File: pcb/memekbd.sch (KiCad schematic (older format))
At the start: 194 parts, among them J1 MJ-4PP-9, J2 MJ-4PP-9, SW1 SW_Push, SW10 SW_Push, SW11 SW_Push, SW12 SW_Push, SW13 SW_Push, SW14 SW_Push, SW15 SW_Push, SW16 SW_Push, SW17 SW_Push, SW18 SW_Push, SW19 SW_Push, SW2 SW_Push, SW20 SW_Push, SW21 SW_Push, SW22 SW_Push, SW23 SW_Push, SW24 SW_Push, SW25 SW_Push, SW26 SW_Push, SW27 SW_Push, SW28 SW_Push, SW29 SW_Push, SW3 SW_Push, SW30 SW_Push, SW31 SW_Push, SW32 SW_Push, SW33 SW_Push, SW34 SW_Push, SW35 SW_Push, SW36 SW_Push, SW37 SW_Push, SW38 SW_Push, SW39 SW_Push, SW4 SW_Push, SW40 SW_Push, SW41 SW_Push, SW42 SW_Push, SW43 SW_Push, SW44 SW_Push, SW45 SW_Push, SW46 SW_Push, SW47 SW_Push, SW48 SW_Push, SW5 SW_Push, SW6 SW_Push, SW7 SW_Push, SW8 SW_Push, SW9 SW_Push, U1 ProMicro, U2 ProMicro

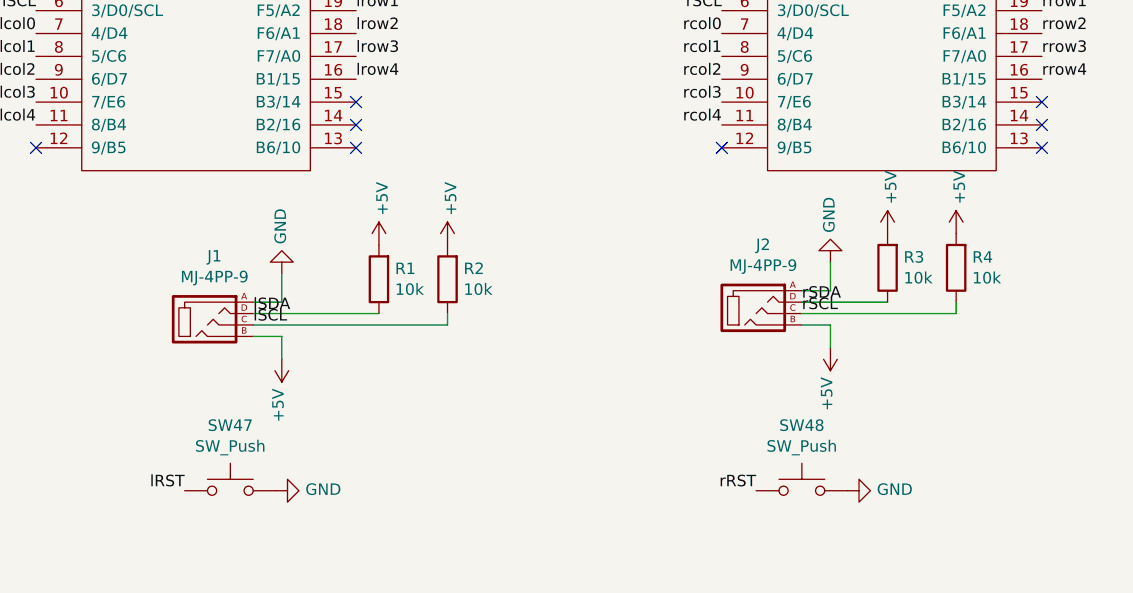
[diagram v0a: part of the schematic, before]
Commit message: Remove unnecessary libraries. Update footprints
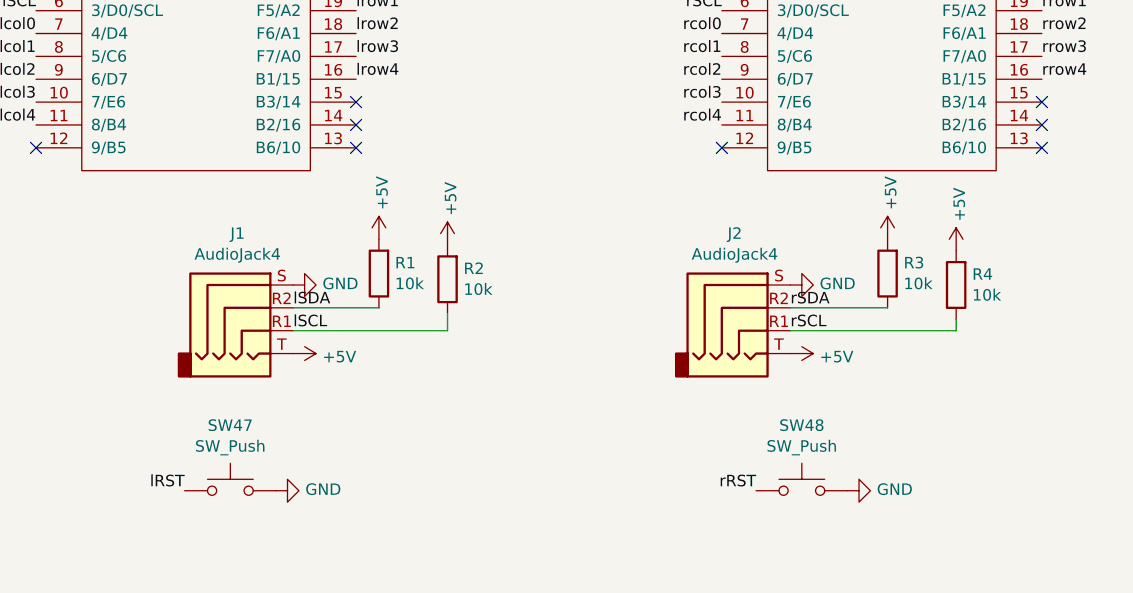
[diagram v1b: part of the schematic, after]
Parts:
- removed J1, J2: MJ-4PP-9, kbd:MJ-4PP-9_1side, symbol kbd:MJ-4PP-9
- added J1, J2: AudioJack4, Connector_Audio:Jack_3.5mm_PJ320D_Horizontal, symbol Connector:AudioJack4
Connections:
- net +5V: now also J1.T, J2.T
- net GND: now also J1.S, J2.S
- net lSCL: now also J1.R1
- net lSDA: now also J1.R2
- net rSCL: now also J2.R1
- net rSDA: now also J2.R2
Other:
- moved on the sheet: R1, R3, R4
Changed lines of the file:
@@
 $EndComp
 $Comp
-L power:GND #PWR0127
-U 1 1 60D9B386
-P 15875 3500
-F 0 "#PWR0127" H 15875 3250 50  0001 C CNN
-F 1 "GND" V 15880 3372 50  0000 R CNN
-F 2 "" H 15875 3500 50  0001 C CNN
-F 3 "" H 15875 3500 50  0001 C CNN
-	1    15875 3500
-	-1   0    0    1
-$EndComp
-$Comp
 L power:GND #PWR0122
 U 1 1 60D9BE71
@@
 $EndComp
 $Comp
-L power:+5V #PWR0128
-U 1 1 60D9D453
-P 15875 3875
-F 0 "#PWR0128" H 15875 3725 50  0001 C CNN
-F 1 "+5V" V 15890 4003 50  0000 L CNN
-F 2 "" H 15875 3875 50  0001 C CNN
-F 3 "" H 15875 3875 50  0001 C CNN
-	1    15875 3875
-	-1   0    0    1
-$EndComp
-$Comp
 L power:GND #PWR0140
 U 1 1 60D9EE51
@@
 $EndComp
 Wire Wire Line
-	16600 3725 16600 3675
-Wire Wire Line
-	15750 3725 16600 3725
-Text Label 15750 3675 0    50   ~ 0
-lSDA
-Text Label 15750 3725 0    50   ~ 0
+	16600 3750 16600 3675
+Text Label 15925 3750 0    50   ~ 0
 lSCL
 Text Label 17800 2250 2    50   ~ 0
@@
 L Device:R R3
 U 1 1 60E5D7AF
-P 18525 3475
-F 0 "R3" H 18455 3429 50  0000 R CNN
-F 1 "10k" H 18455 3520 50  0000 R CNN
-F 2 "Resistor_THT:R_Axial_DIN0207_L6.3mm_D2.5mm_P7.62mm_Horizontal" V 18455 3475 50  0001 C CNN
-F 3 "~" H 18525 3475 50  0001 C CNN
-	1    18525 3475
+P 18525 3500
+F 0 "R3" H 18455 3454 50  0000 R CNN
+F 1 "10k" H 18455 3545 50  0000 R CNN
+F 2 "Resistor_THT:R_Axial_DIN0207_L6.3mm_D2.5mm_P7.62mm_Horizontal" V 18455 3500 50  0001 C CNN
+F 3 "~" H 18525 3500 50  0001 C CNN
+	1    18525 3500
 	-1   0    0    1
 $EndComp
@@
 L power:+5V #PWR0138
 U 1 1 60E5D7B5
-P 18525 3325
-F 0 "#PWR0138" H 18525 3175 50  0001 C CNN
-F 1 "+5V" V 18540 3453 50  0000 L CNN
-F 2 "" H 18525 3325 50  0001 C CNN
-F 3 "" H 18525 3325 50  0001 C CNN
-	1    18525 3325
+P 18525 3350
+F 0 "#PWR0138" H 18525 3200 50  0001 C CNN
+F 1 "+5V" V 18540 3478 50  0000 L CNN
+F 2 "" H 18525 3350 50  0001 C CNN
+F 3 "" H 18525 3350 50  0001 C CNN
+	1    18525 3350
 	1    0    0    -1
 $EndComp
@@
 L Device:R R4
 U 1 1 60E5D7BB
-P 18825 3475
-F 0 "R4" H 18755 3429 50  0000 R CNN
-F 1 "10k" H 18755 3520 50  0000 R CNN
-F 2 "Resistor_THT:R_Axial_DIN0207_L6.3mm_D2.5mm_P7.62mm_Horizontal" V 18755 3475 50  0001 C CNN
-F 3 "~" H 18825 3475 50  0001 C CNN
-	1    18825 3475
+P 18825 3550
+F 0 "R4" H 18755 3504 50  0000 R CNN
+F 1 "10k" H 18755 3595 50  0000 R CNN
+F 2 "Resistor_THT:R_Axial_DIN0207_L6.3mm_D2.5mm_P7.62mm_Horizontal" V 18755 3550 50  0001 C CNN
+F 3 "~" H 18825 3550 50  0001 C CNN
+	1    18825 3550
 	-1   0    0    1
 $EndComp
@@
 L power:+5V #PWR0139
 U 1 1 60E5D7C1
-P 18825 3325
-F 0 "#PWR0139" H 18825 3175 50  0001 C CNN
-F 1 "+5V" V 18840 3453 50  0000 L CNN
-F 2 "" H 18825 3325 50  0001 C CNN
-F 3 "" H 18825 3325 50  0001 C CNN
-	1    18825 3325
+P 18825 3400
+F 0 "#PWR0139" H 18825 3250 50  0001 C CNN
+F 1 "+5V" V 18840 3528 50  0000 L CNN
+F 2 "" H 18825 3400 50  0001 C CNN
+F 3 "" H 18825 3400 50  0001 C CNN
+	1    18825 3400
 	1    0    0    -1
 $EndComp
 Wire Wire Line
-	18825 3675 18825 3625
+	18825 3750 18825 3700
 Wire Wire Line
-	18150 3675 18825 3675
+	18100 3750 18825 3750
 Wire Wire Line
-	18150 3625 18525 3625
-Text Label 18150 3625 0    50   ~ 0
+	18100 3650 18525 3650
+Text Label 18100 3650 0    50   ~ 0
 rSDA
-Text Label 18150 3675 0    50   ~ 0
+Text Label 18100 3750 0    50   ~ 0
 rSCL
 Text Label 2100 7000 2    50   ~ 0
@@
 NoConn ~ 19200 1850
 $Comp
-L kbd:MJ-4PP-9 J1
-U 1 1 614F36EF
-P 15550 3700
-F 0 "J1" H 15581 3976 50  0000 C CNN
-F 1 "MJ-4PP-9" H 15581 3885 50  0000 C CNN
-F 2 "kbd:MJ-4PP-9_1side" H 15825 3875 50  0001 C CNN
-F 3 "~" H 15825 3875 50  0001 C CNN
-	1    15550 3700
-	1    0    0    -1
+L power:+5V #PWR0136
+U 1 1 615CFE82
+P 18100 3850
+F 0 "#PWR0136" H 18100 3700 50  0001 C CNN
+F 1 "+5V" V 18115 3978 50  0000 L CNN
+F 2 "" H 18100 3850 50  0001 C CNN
+F 3 "" H 18100 3850 50  0001 C CNN
+	1    18100 3850
+	0    1    1    0
 $EndComp
 $Comp
-L kbd:MJ-4PP-9 J2
-U 1 1 614F5099
-P 17950 3650
-F 0 "J2" H 17981 3926 50  0000 C CNN
-F 1 "MJ-4PP-9" H 17981 3835 50  0000 C CNN
-F 2 "kbd:MJ-4PP-9_1side" H 18225 3825 50  0001 C CNN
-F 3 "~" H 18225 3825 50  0001 C CNN
-	1    17950 3650
+L power:GND #PWR0137
+U 1 1 615D8D20
+P 18100 3550
+F 0 "#PWR0137" H 18100 3300 50  0001 C CNN
+F 1 "GND" V 18105 3422 50  0000 R CNN
+F 2 "" H 18100 3550 50  0001 C CNN
+F 3 "" H 18100 3550 50  0001 C CNN
+	1    18100 3550
+	0    -1   -1   0
+$EndComp
+$Comp
+L Connector:AudioJack4 J2
+U 1 1 60C1F37A
+P 17900 3650
+F 0 "J2" H 17857 3975 50  0000 C CNN
+F 1 "AudioJack4" H 17857 3884 50  0000 C CNN
+F 2 "Connector_Audio:Jack_3.5mm_PJ320D_Horizontal" H 17900 3650 50  0001 C CNN
+F 3 "~" H 17900 3650 50  0001 C CNN
+	1    17900 3650
 	1    0    0    -1
 $EndComp
-Wire Wire Line
-	15750 3625 15875 3625
-Wire Wire Line
-	15875 3625 15875 3500
-Wire Wire Line
-	15750 3775 15875 3775
-Wire Wire Line
-	15875 3775 15875 3875
-Wire Wire Line
-	15750 3675 16300 3675
 $Comp
 L power:+5V #PWR0131
 U 1 1 60DFD705
-P 16300 3375
-F 0 "#PWR0131" H 16300 3225 50  0001 C CNN
-F 1 "+5V" V 16315 3503 50  0000 L CNN
-F 2 "" H 16300 3375 50  0001 C CNN
-F 3 "" H 16300 3375 50  0001 C CNN
-	1    16300 3375
+P 16300 3350
+F 0 "#PWR0131" H 16300 3200 50  0001 C CNN
+F 1 "+5V" V 16315 3478 50  0000 L CNN
+F 2 "" H 16300 3350 50  0001 C CNN
+F 3 "" H 16300 3350 50  0001 C CNN
+	1    16300 3350
 	1    0    0    -1
 $EndComp
@@
 L Device:R R1
 U 1 1 60DFBED0
-P 16300 3525
-F 0 "R1" H 16230 3479 50  0000 R CNN
-F 1 "10k" H 16230 3570 50  0000 R CNN
-F 2 "Resistor_THT:R_Axial_DIN0207_L6.3mm_D2.5mm_P7.62mm_Horizontal" V 16230 3525 50  0001 C CNN
-F 3 "~" H 16300 3525 50  0001 C CNN
-	1    16300 3525
+P 16300 3500
+F 0 "R1" H 16230 3454 50  0000 R CNN
+F 1 "10k" H 16230 3545 50  0000 R CNN
+F 2 "Resistor_THT:R_Axial_DIN0207_L6.3mm_D2.5mm_P7.62mm_Horizontal" V 16230 3500 50  0001 C CNN
+F 3 "~" H 16300 3500 50  0001 C CNN
+	1    16300 3500
 	-1   0    0    1
 $EndComp
+Text Label 15925 3650 0    50   ~ 0
+lSDA
 $Comp
-L power:+5V #PWR0136
-U 1 1 615CFE82
-P 18275 3825
-F 0 "#PWR0136" H 18275 3675 50  0001 C CNN
-F 1 "+5V" V 18290 3953 50  0000 L CNN
-F 2 "" H 18275 3825 50  0001 C CNN
-F 3 "" H 18275 3825 50  0001 C CNN
-	1    18275 3825
-	-1   0    0    1
+L power:+5V #PWR0128
+U 1 1 60D9D453
+P 15925 3850
+F 0 "#PWR0128" H 15925 3700 50  0001 C CNN
+F 1 "+5V" V 15940 3978 50  0000 L CNN
+F 2 "" H 15925 3850 50  0001 C CNN
+F 3 "" H 15925 3850 50  0001 C CNN
+	1    15925 3850
+	0    1    1    0
 $EndComp
-Wire Wire Line
-	18150 3725 18275 3725
-Wire Wire Line
-	18275 3725 18275 3825
 $Comp
-L power:GND #PWR0137
-U 1 1 615D8D20
-P 18275 3450
-F 0 "#PWR0137" H 18275 3200 50  0001 C CNN
-F 1 "GND" V 18280 3322 50  0000 R CNN
-F 2 "" H 18275 3450 50  0001 C CNN
-F 3 "" H 18275 3450 50  0001 C CNN
-	1    18275 3450
-	-1   0    0    1
+L power:GND #PWR0127
+U 1 1 60D9B386
+P 15925 3550
+F 0 "#PWR0127" H 15925 3300 50  0001 C CNN
+F 1 "GND" V 15930 3422 50  0000 R CNN
+F 2 "" H 15925 3550 50  0001 C CNN
+F 3 "" H 15925 3550 50  0001 C CNN
+	1    15925 3550
+	0    -1   -1   0
 $EndComp
 Wire Wire Line
-	18275 3575 18275 3450
-Wire Wire Line
-	18275 3575 18150 3575
+	15925 3650 16300 3650
+Wire Wire Line
+	15925 3750 16600 3750
+$Comp
+L Connector:AudioJack4 J1
+U 1 1 60C1B4D6
+P 15725 3650
+F 0 "J1" H 15682 3975 50  0000 C CNN
+F 1 "AudioJack4" H 15682 3884 50  0000 C CNN
+F 2 "Connector_Audio:Jack_3.5mm_PJ320D_Horizontal" H 15725 3650 50  0001 C CNN
+F 3 "~" H 15725 3650 50  0001 C CNN
+	1    15725 3650
+	1    0    0    -1
+$EndComp
 $EndSCHEMATC

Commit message: Some routing
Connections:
- net lSCL: now also J1.R2, R1.1; no longer J1.R1, R2.1
- net lSDA: now also J1.R1, R2.1; no longer J1.R2, R1.1
- net rSCL: now also J2.R2, R3.1; no longer J2.R1, R4.1
- net rSDA: now also J2.R1, R4.1; no longer J2.R2, R3.1
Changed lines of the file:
@@
 Wire Wire Line
 	16600 3750 16600 3675
-Text Label 15925 3750 0    50   ~ 0
+Text Label 15925 3650 0    50   ~ 0
 lSCL
 Text Label 17800 2250 2    50   ~ 0
@@
 Wire Wire Line
 	18100 3650 18525 3650
+Text Label 18100 3750 0    50   ~ 0
+rSDA
 Text Label 18100 3650 0    50   ~ 0
-rSDA
-Text Label 18100 3750 0    50   ~ 0
 rSCL
 Text Label 2100 7000 2    50   ~ 0
@@
 	-1   0    0    1
 $EndComp
-Text Label 15925 3650 0    50   ~ 0
+Text Label 15925 3750 0    50   ~ 0
 lSDA
 $Comp

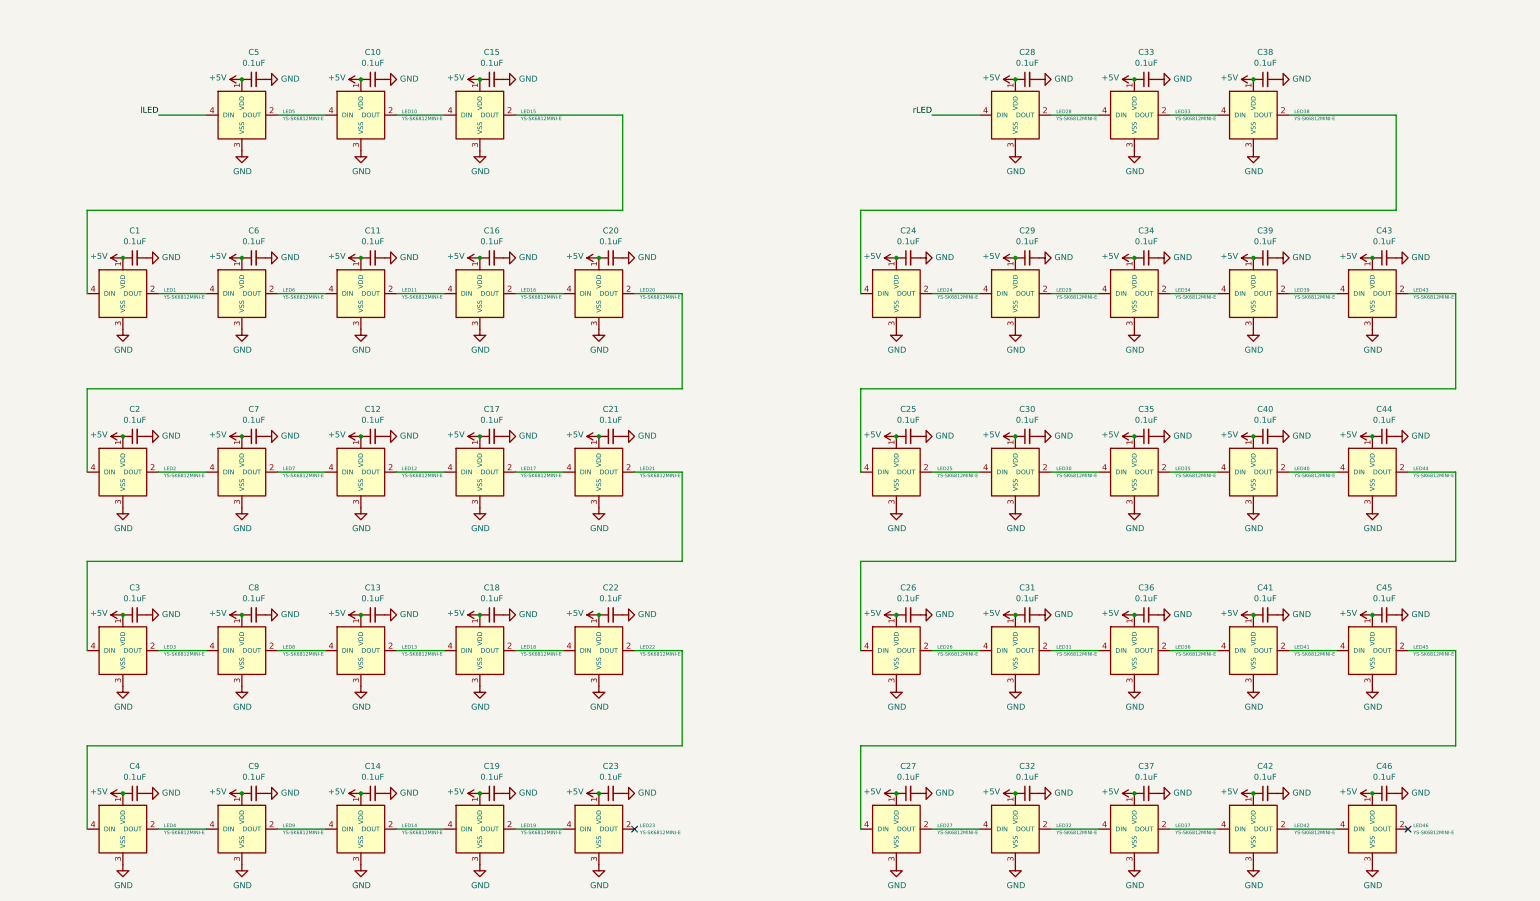
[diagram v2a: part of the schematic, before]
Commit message: Some LED changes.
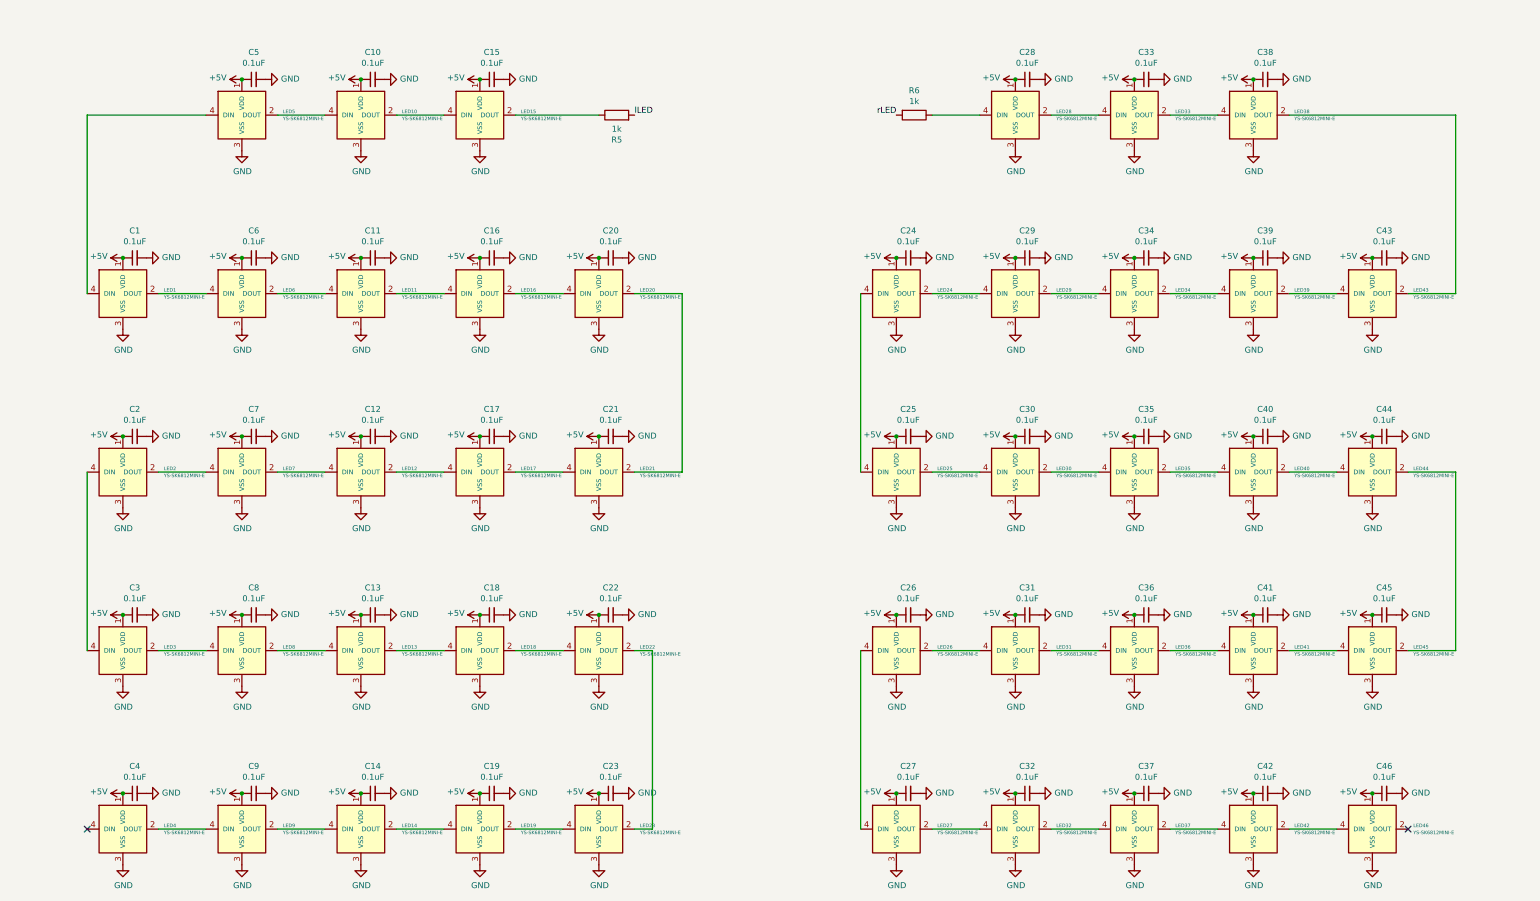
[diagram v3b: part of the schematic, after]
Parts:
- added R5, R6: 1k, Resistor_THT:R_Axial_DIN0207_L6.3mm_D2.5mm_P7.62mm_Horizontal, symbol Device:R
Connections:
- net lLED: now also R5.2; no longer LED5.4 (DIN)
- net rLED: now also R6.2; no longer LED28.4 (DIN)
- net at LED1.4 (DIN): now also LED5.4 (DIN); no longer LED15.2 (DOUT)
- net at LED20.2 (DOUT): now also LED21.2 (DOUT); no longer LED2.4 (DIN)
- net at LED3.4 (DIN): now also LED2.4 (DIN); no longer LED21.2 (DOUT)
- net at LED22.2 (DOUT): now also LED23.2 (DOUT); no longer LED4.4 (DIN)
- net at LED24.4 (DIN): now also LED25.4 (DIN); no longer LED38.2 (DOUT)
- net at LED43.2 (DOUT): now also LED38.2 (DOUT); no longer LED25.4 (DIN)
- net at LED44.2 (DOUT): now also LED45.2 (DOUT); no longer LED26.4 (DIN)
- net at LED27.4 (DIN): now also LED26.4 (DIN); no longer LED45.2 (DOUT)
- new net: LED15.2 (DOUT), R5.1
- new net: LED28.4 (DIN), R6.1
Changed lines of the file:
@@
 $EndComp
 Wire Wire Line
-	2100 7000 2500 7000
-Wire Wire Line
 	3100 7000 3500 7000
 Wire Wire Line
@@
 	4100 8500 4500 8500
 Wire Wire Line
-	5100 7000 6000 7000
-Wire Wire Line
-	6000 7000 6000 7800
-Wire Wire Line
-	6000 7800 1500 7800
-Wire Wire Line
-	1500 7800 1500 8500
-Wire Wire Line
 	6100 8500 6500 8500
 Wire Wire Line
-	6500 8500 6500 9300
-Wire Wire Line
-	6500 9300 1500 9300
-Wire Wire Line
-	1500 9300 1500 10000
-Wire Wire Line
 	6100 10000 6500 10000
 Wire Wire Line
-	6500 10000 6500 10750
-Wire Wire Line
-	6500 10750 1500 10750
-Wire Wire Line
-	1500 10750 1500 11500
-Wire Wire Line
-	6100 11500 6500 11500
-Wire Wire Line
-	6500 11500 6500 12300
-Wire Wire Line
-	6500 12300 1500 12300
-Wire Wire Line
-	1500 12300 1500 13000
-NoConn ~ 6100 13000
-Wire Wire Line
 	8600 7000 9000 7000
 Wire Wire Line
-	11600 7000 12500 7000
-Wire Wire Line
-	12500 7000 12500 7800
-Wire Wire Line
-	12500 7800 8000 7800
-Wire Wire Line
-	8000 7800 8000 8500
-Wire Wire Line
-	13000 8500 13000 9300
-Wire Wire Line
-	13000 9300 8000 9300
-Wire Wire Line
-	8000 9300 8000 10000
-Wire Wire Line
 	12600 10000 13000 10000
 Wire Wire Line
-	13000 10000 13000 10750
-Wire Wire Line
-	13000 10750 8000 10750
-Wire Wire Line
-	8000 10750 8000 11500
-Wire Wire Line
 	12600 11500 13000 11500
-Wire Wire Line
-	13000 11500 13000 12300
-Wire Wire Line
-	13000 12300 8000 12300
-Wire Wire Line
-	8000 12300 8000 13000
 NoConn ~ 12600 13000
 $Comp
@@
 Text Label 18100 3650 0    50   ~ 0
 rSCL
-Text Label 2100 7000 2    50   ~ 0
+Text Label 6100 7000 0    50   ~ 0
 lLED
-Text Label 8600 7000 2    50   ~ 0
+Text Label 8300 7000 2    50   ~ 0
 rLED
 Text Label 14800 1850 2    50   ~ 0
@@
 	1    0    0    -1
 $EndComp
+$Comp
+L Device:R R5
+U 1 1 60E55CD7
+P 5950 7000
+F 0 "R5" V 5743 7000 50  0000 C CNN
+F 1 "1k" V 5834 7000 50  0000 C CNN
+F 2 "Resistor_THT:R_Axial_DIN0207_L6.3mm_D2.5mm_P7.62mm_Horizontal" V 5880 7000 50  0001 C CNN
+F 3 "~" H 5950 7000 50  0001 C CNN
+	1    5950 7000
+	0    -1   -1   0
+$EndComp
+$Comp
+L Device:R R6
+U 1 1 60E6C693
+P 8450 7000
+F 0 "R6" V 8243 7000 50  0000 C CNN
+F 1 "1k" V 8334 7000 50  0000 C CNN
+F 2 "Resistor_THT:R_Axial_DIN0207_L6.3mm_D2.5mm_P7.62mm_Horizontal" V 8380 7000 50  0001 C CNN
+F 3 "~" H 8450 7000 50  0001 C CNN
+	1    8450 7000
+	0    1    1    0
+$EndComp
+Wire Wire Line
+	5800 7000 5100 7000
+Wire Wire Line
+	2500 7000 1500 7000
+Wire Wire Line
+	1500 7000 1500 8500
+Wire Wire Line
+	6500 8500 6500 10000
+Wire Wire Line
+	1500 10000 1500 11500
+NoConn ~ 1500 13000
+Wire Wire Line
+	6250 11500 6250 13000
+Wire Wire Line
+	6250 13000 6100 13000
+Wire Wire Line
+	6100 11500 6250 11500
+Wire Wire Line
+	13000 7000 13000 8500
+Wire Wire Line
+	11600 7000 13000 7000
+Wire Wire Line
+	8000 8500 8000 10000
+Wire Wire Line
+	13000 10000 13000 11500
+Wire Wire Line
+	8000 11500 8000 13000
 $EndSCHEMATC
